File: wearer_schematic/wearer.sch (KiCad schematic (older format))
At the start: 19 parts

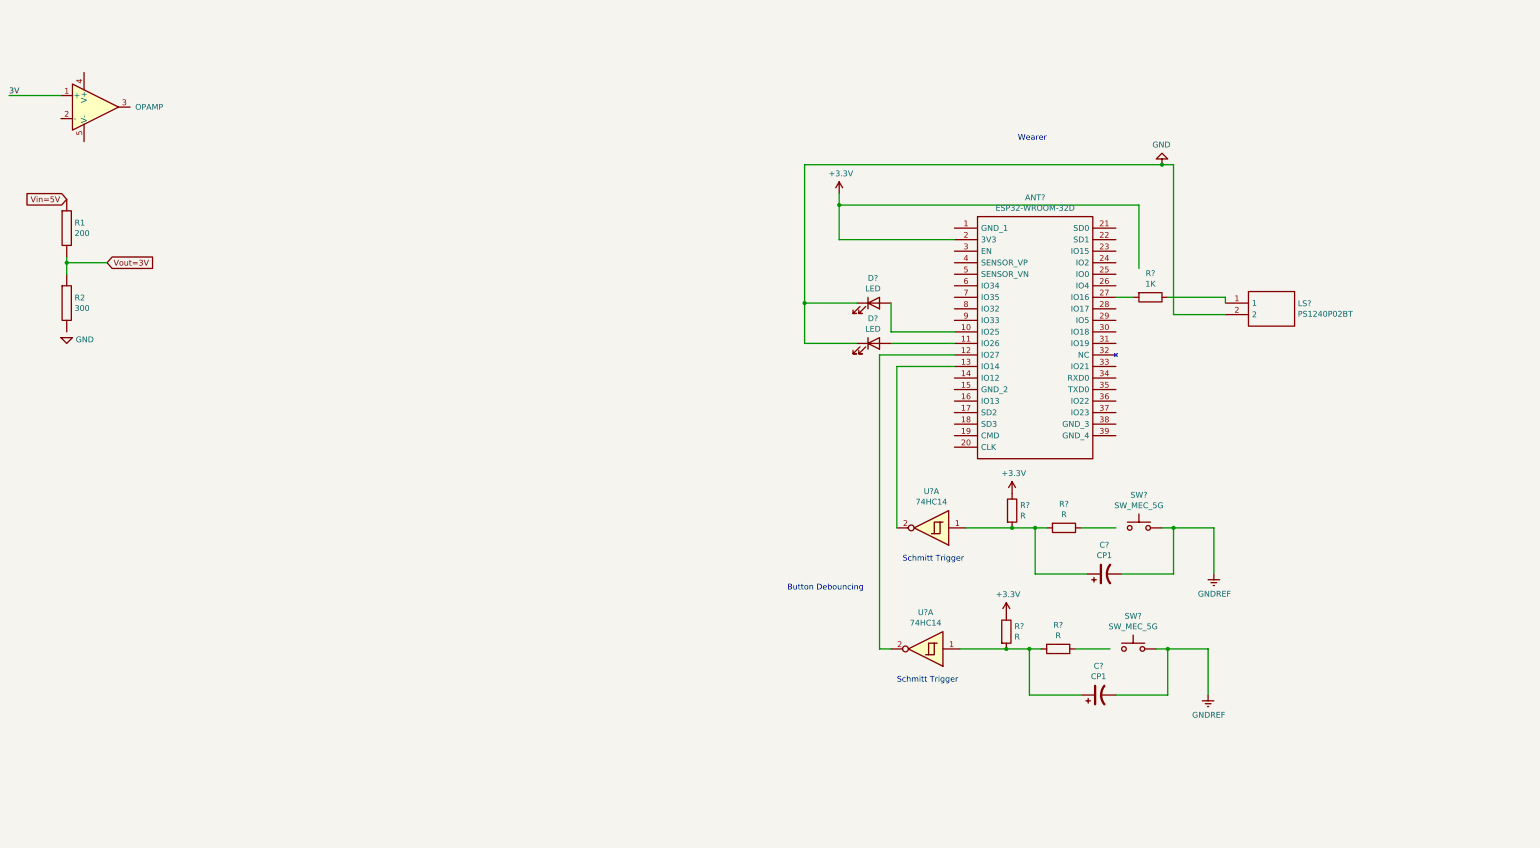
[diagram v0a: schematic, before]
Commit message: added to schematic
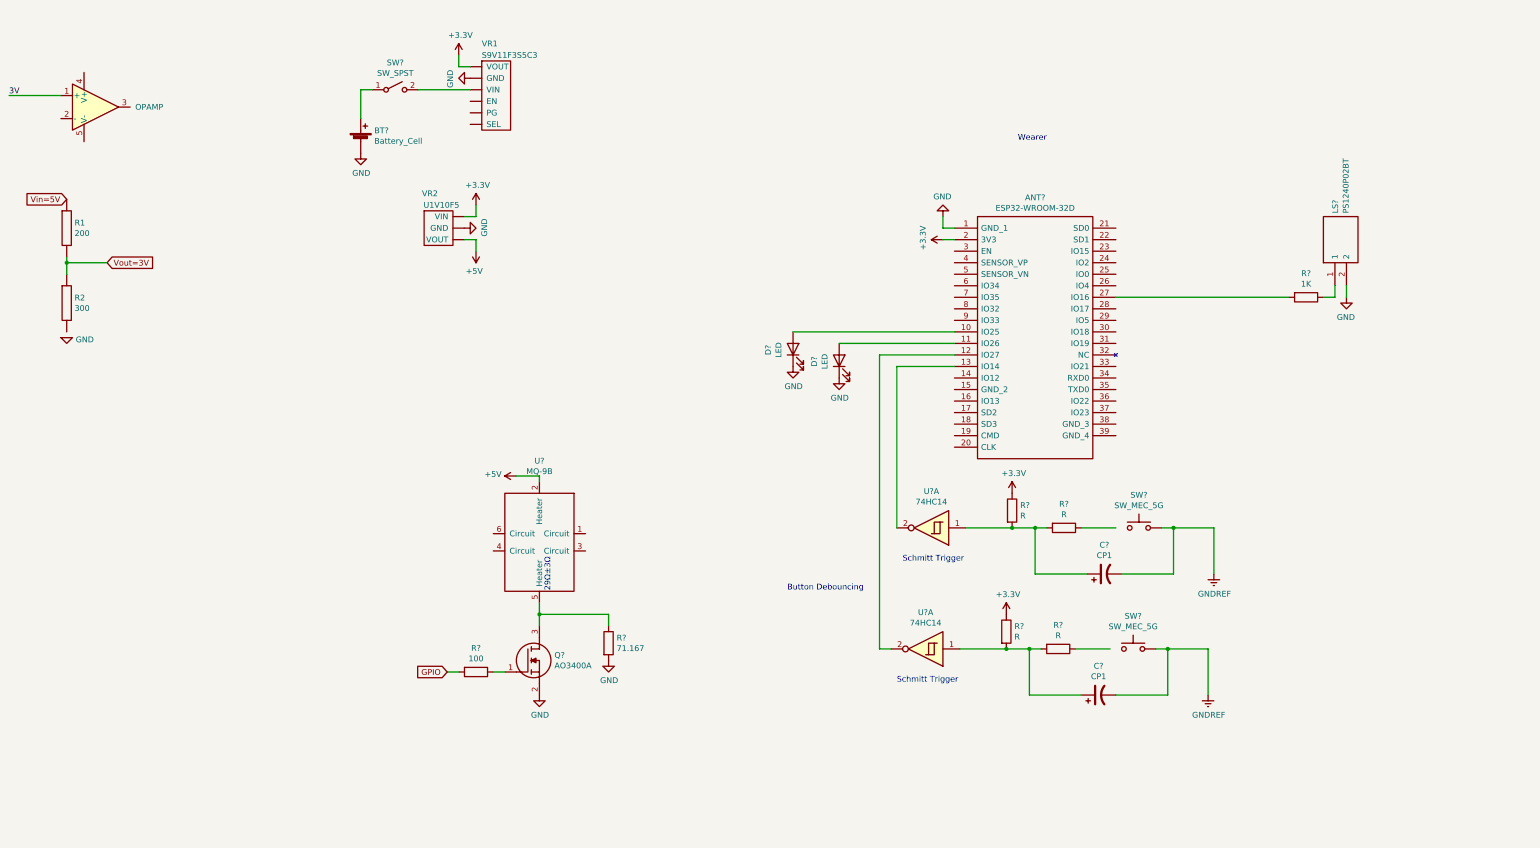
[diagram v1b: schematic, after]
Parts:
- added BT?: Battery_Cell, symbol Device:Battery_Cell
- added Q?: AO3400A, SOT95P280X125-3N, symbol Noggin:AO3400A
- added R?: 100, symbol Device:R
- added R?: 71.167, symbol Device:R
- added SW?: SW_SPST, symbol Switch:SW_SPST
- added U?: MQ-9B, symbol Noggin:MQ-9B
- added VR1: S9V11F3S5C3, symbol Noggin:S9V11F3S5C3
- added VR2: U1V10F5, symbol Noggin:U1V10F5
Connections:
- net +3V3: now also VR1.~ (VOUT), VR2.~ (VOUT)
- net GND: now also ANT?.1 (GND_1), BT?.2 (-), Q?.2, R?.2, VR1.~ (VOUT), VR2.~ (VOUT)
- new net: SW?.2 (B), VR1.~ (VOUT)
- new net: BT?.1 (+), SW?.1 (A)
- new net: Q?.3, R?.1, U?.5 (Heater)
- new net: Q?.1, R?.1
- new net +5V: U?.2 (Heater), VR2.~ (VOUT)
- new net GPIO: R?.2
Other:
- note added: "29Ω±3Ω"
- moved on the sheet: D?, LS?, R?

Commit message: updated wearer schematic
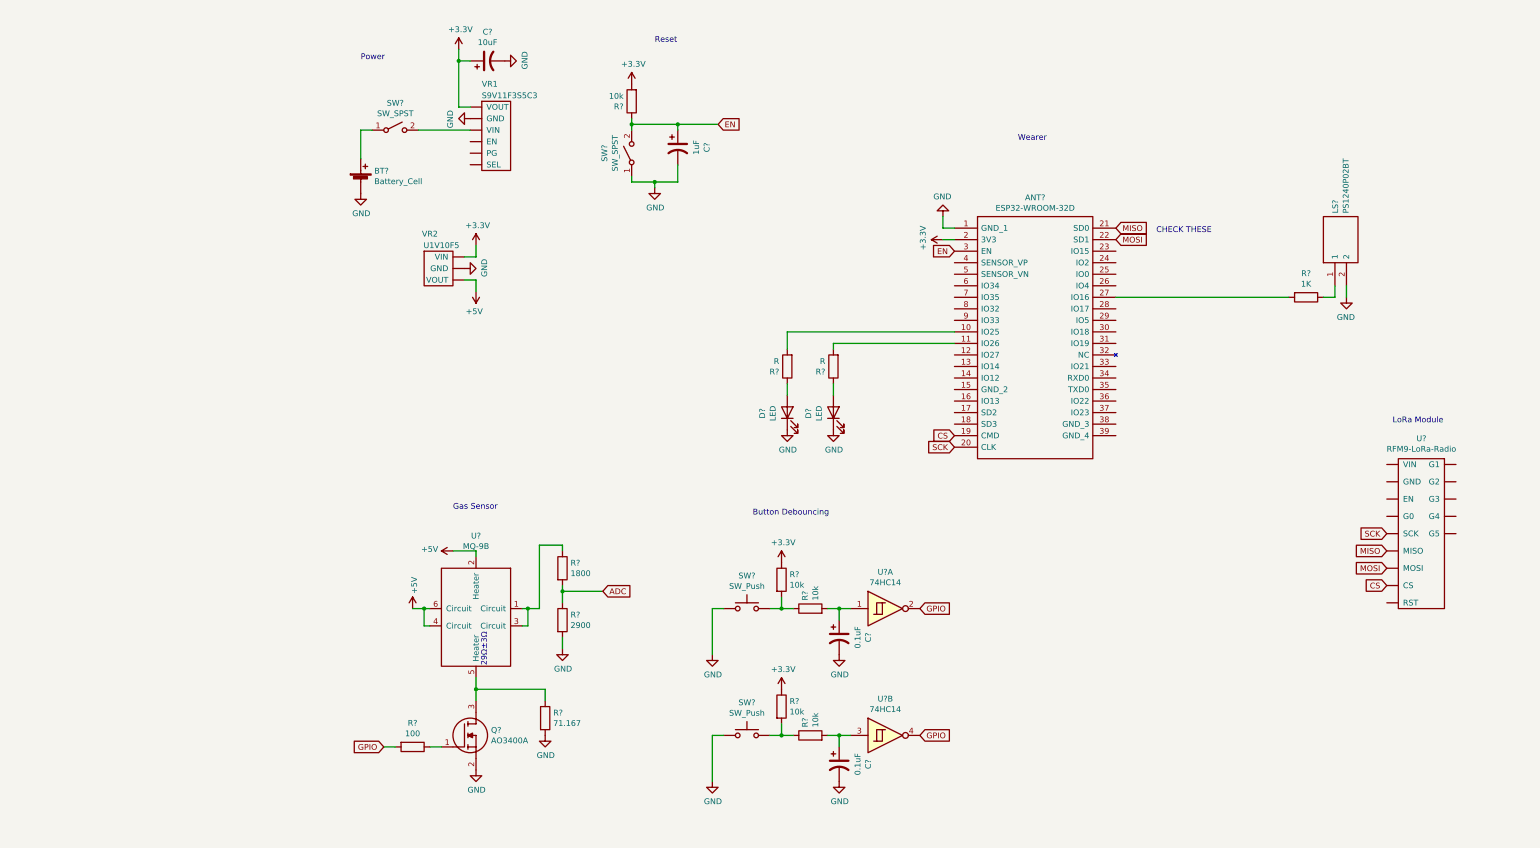
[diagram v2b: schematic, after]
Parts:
- removed C? (x2): CP1, symbol Device:CP1
- removed GND: 0, symbol pspice:0
- removed OpAmp1: OPAMP, symbol pspice:OPAMP
- removed R1: 200, symbol pspice:R
- removed R2: 300, symbol pspice:R
- removed R? (x4): R, symbol Device:R
- removed SW? (x2): SW_MEC_5G, symbol Switch:SW_MEC_5G
- removed U? (x2): 74HC14, symbol 74xx:74HC14
- added C?: 10uF, symbol Device:CP1
- added C? (x2): 0.1uF, symbol Device:CP1
- added C?: 1uF, symbol Device:CP1
- added R? (x2): R, symbol Device:R
- added R?: 1800, symbol Device:R
- added R?: 2900, symbol Device:R
- added R? (x5): 10k, symbol Device:R
- added SW? (x2): SW_Push, symbol Switch:SW_Push
- added SW?: SW_SPST, symbol Switch:SW_SPST
- added U?: RFM9-LoRa-Radio, symbol Noggin:RFM9-LoRa-Radio
- added U? (x2): 74HC14, symbol 74xx:74HC14
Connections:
- net +3V3: now also C?.1, R?.1, R?.1, R?.2
- net +5V: now also U?.4 (Circuit), U?.6 (Circuit)
- net GND: now also C?.2, C?.2, C?.2, C?.2, R?.2, SW?.1, SW?.1, SW?.1 (A)
- net GPIO: now also U?.2, U?.4
- net at ANT?.10 (IO25): now also R?.2; no longer D?.2 (A)
- net at ANT?.11 (IO26): now also R?.2; no longer D?.2 (A)
- net CS: now reaches ANT?.19 (CMD)
- net CS: now also U?.~ (VIN)
- net SCK: now reaches ANT?.20 (CLK)
- net SCK: now also U?.~ (VIN)
- net MISO: now reaches ANT?.21 (SD0)
- net MISO: now also U?.~ (VIN)
- net MOSI: now reaches ANT?.22 (SD1)
- net MOSI: now also U?.~ (VIN)
- net EN: now reaches ANT?.3 (EN)
- net EN: now also C?.1, R?.1, SW?.2 (B)
- net at U?.1 (Circuit): now also U?.3 (Circuit), R?.1
- new net: D?.2 (A), R?.1 (x2)
- new net: C?.1, R?.2, U?.1
- new net: C?.1, R?.2, U?.3
- new net: R?.1, R?.2, SW?.2 (x2)
- new net ADC: R?.1, R?.2
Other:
- note added: "Button Debouncing"
- note added: "CHECK THESE"
- note added: "Gas Sensor"
- note added: "LoRa Module"
- note added: "Power"
- note added: "Reset"
- note removed: "Button Debouncing\n"
- note removed: "Schmitt Trigger\n"
- moved on the sheet: BT?, D?, Q?, R?, SW?, U?, VR1, VR2

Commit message: update schematic
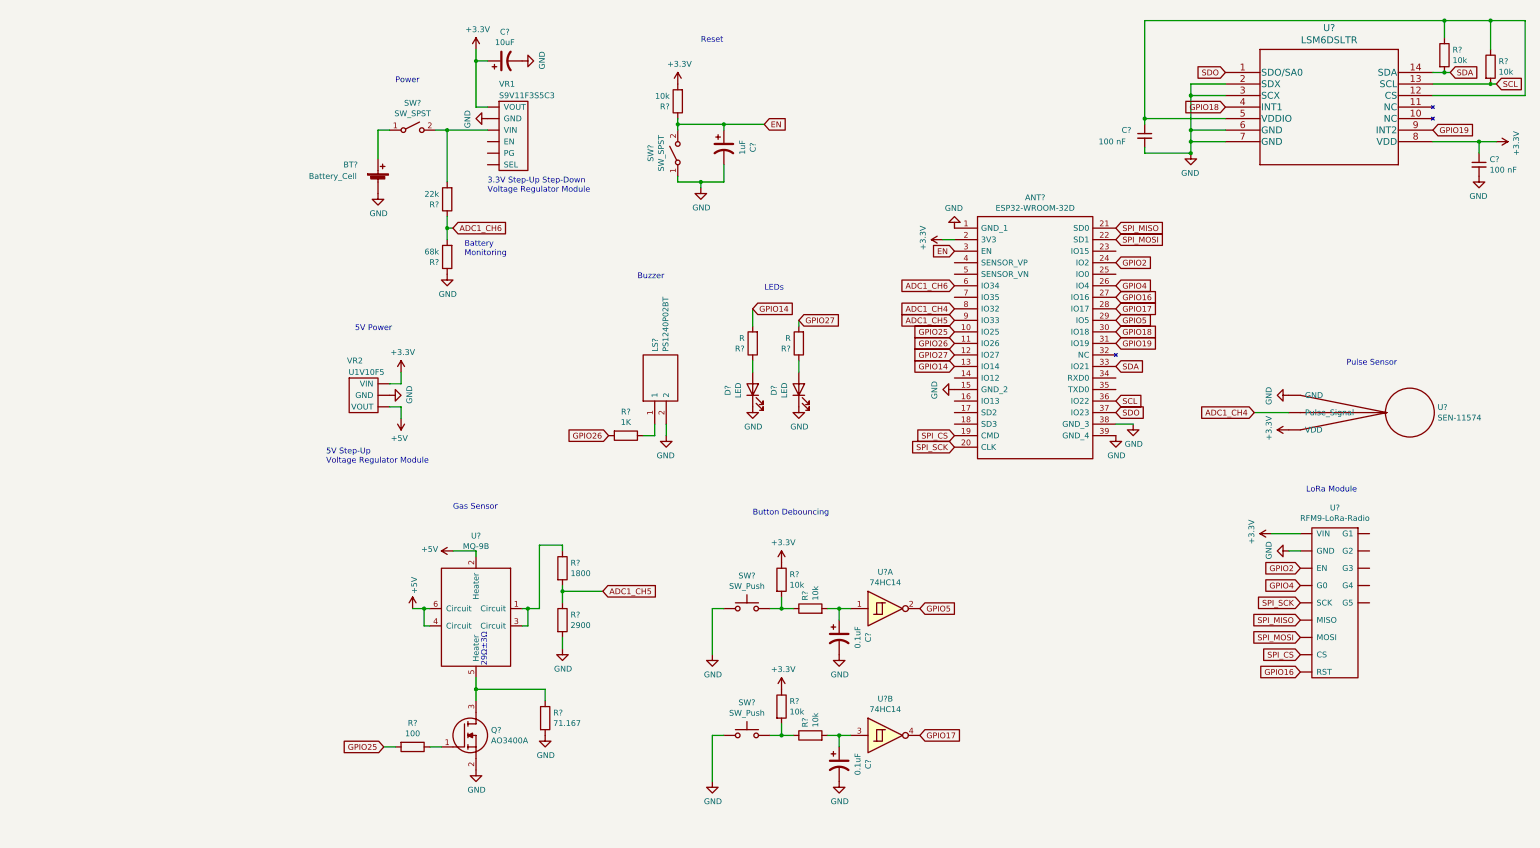
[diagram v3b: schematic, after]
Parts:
- added C? (x2): 100 nF, symbol Device:C_Small
- added R? (x2): 10k, symbol Device:R
- added R?: 22k, symbol Device:R
- added R?: 68k, symbol Device:R
- added U?: LSM6DSLTR, QFN_6DSLTR_STM, symbol Noggin:LSM6DSLTR
- added U?: SEN-11574, symbol Noggin:SEN-11574
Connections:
- net ADC is gone; now on net ADC1_CH5: R?.1, R?.2
- net SCK is gone; now on net SPI_SCK: ANT?.20 (CLK), U?.~ (VIN)
- net +3V3: now also U?.~ (VIN), C?.1, U?.8 (VDD), U?.~ (VDD)
- net GND: now also ANT?.15 (GND_2), ANT?.38 (GND_3), ANT?.39 (GND_4), U?.~ (VIN), C?.2, C?.2, R?.1, U?.2 (SDX), U?.3 (SCX), U?.6 (GND), U?.7 (GND), U?.~ (VDD)
- net GPIO14: now reaches R?.2
- net GPIO14: now also ANT?.13 (IO14); no longer ANT?.10 (IO25)
- net GPIO26: now reaches ANT?.11 (IO26)
- net GPIO26: now also R?.2; no longer R?.2
- net GPIO27: now reaches ANT?.12 (IO27)
- net GPIO27: now also R?.2
- net GPIO2: now reaches ANT?.24 (IO2)
- net GPIO2: now also U?.~ (VIN)
- net GPIO4: now reaches ANT?.26 (IO4)
- net GPIO4: now also U?.~ (VIN)
- net GPIO16: now reaches ANT?.27 (IO16)
- net GPIO16: now also U?.~ (VIN); no longer R?.2
- net GPIO17: now reaches ANT?.28 (IO17)
- net GPIO17: now also U?.4
- net GPIO5: now reaches ANT?.29 (IO5)
- net GPIO5: now also U?.2
- net GPIO18: now reaches ANT?.30 (IO18)
- net GPIO18: now also U?.4 (INT1)
- net GPIO19: now reaches ANT?.31 (IO19)
- net GPIO19: now also U?.9 (INT2)
- net SDA: now reaches ANT?.33 (IO21)
- net SDA: now also R?.2, U?.14 (SDA)
- net SCL: now reaches ANT?.36 (IO22)
- net SCL: now also R?.2, U?.13 (SCL)
- net SDO: now reaches ANT?.37 (IO23)
- net SDO: now also U?.1 (SDO/SA0)
- net ADC1_CH6: now reaches ANT?.6 (IO34)
- net ADC1_CH6: now also R?.1, R?.2
- net ADC1_CH4: now reaches ANT?.8 (IO32)
- net ADC1_CH4: now also U?.~ (VDD)
- net ADC1_CH5: now reaches ANT?.9 (IO33)
- net at SW?.2 (B), VR1.~ (VOUT): now also R?.2
- net SPI_SCK: now reaches U?.~ (VIN)
- net CS renamed SPI_CS
- removed net GPIO: R?.2, U?.2, U?.4
- net MISO renamed SPI_MISO
- net MOSI renamed SPI_MOSI
- new net: C?.1, R?.1, R?.1, U?.12 (CS), U?.5 (VDDIO)
- new net GPIO25: ANT?.10 (IO25), R?.2
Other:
- note added: "3.3V Step-Up Step-Down\nVoltage Regulator Module"
- note added: "5V Power"
- note added: "5V Step-Up\nVoltage Regulator Module"
- note added: "Battery\nMonitoring"
- note added: "Buzzer"
- note added: "LEDs"
- note added: "Pulse Sensor"
- note removed: "CHECK THESE"
- note removed: "Wearer\n"
- moved on the sheet: BT?, C?, D?, LS?, R?, SW?, U?, VR1, VR2

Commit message: update debouncing
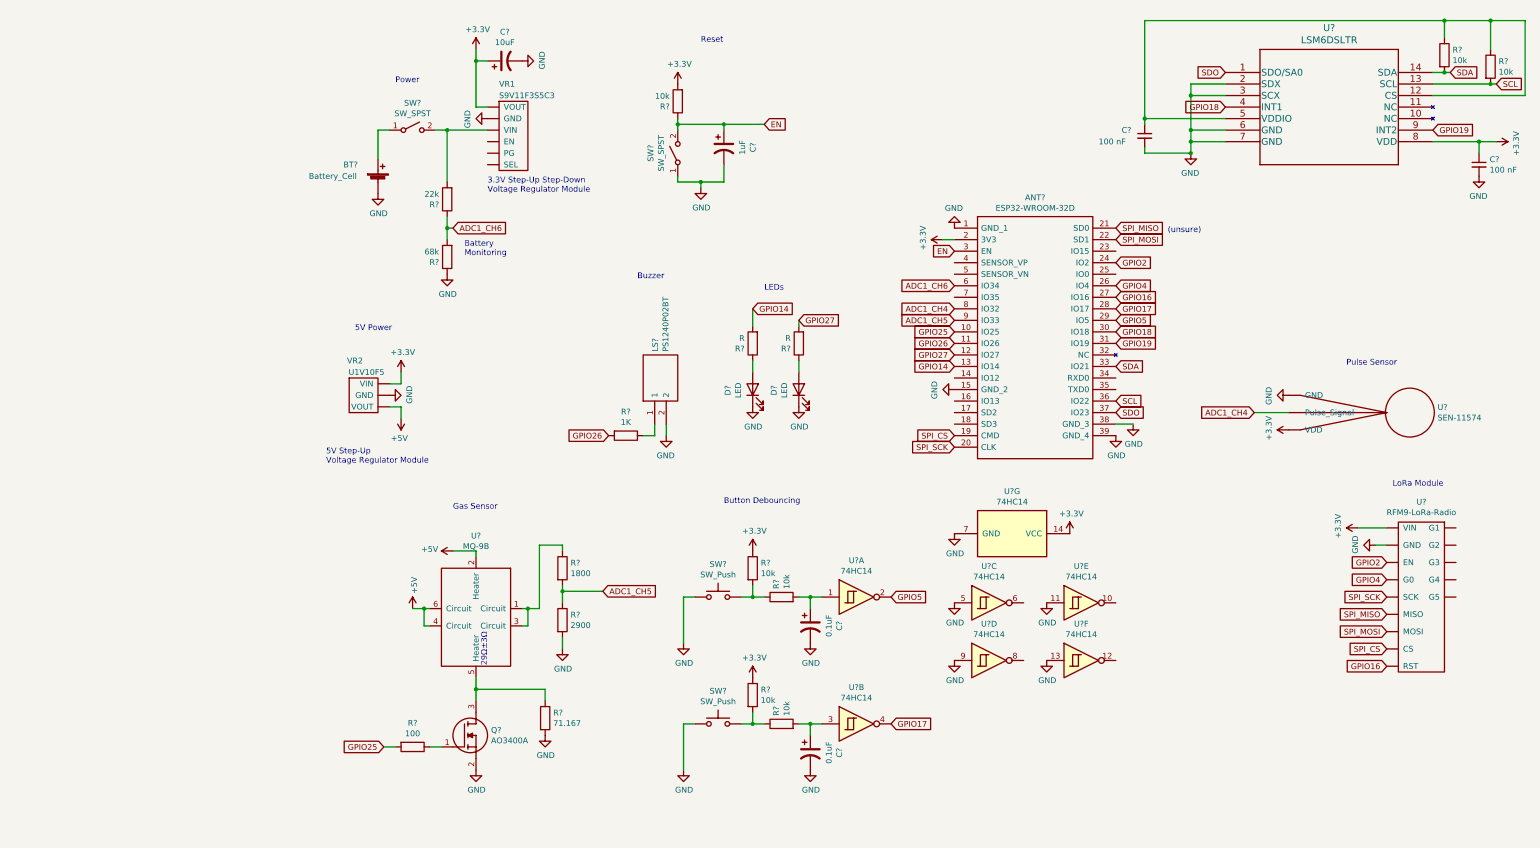
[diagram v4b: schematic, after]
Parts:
- added U? (x5): 74HC14, symbol 74xx:74HC14
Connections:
- net +3V3: now also U?.14 (VCC)
- net GND: now also U?.11, U?.13, U?.5, U?.7 (GND), U?.9
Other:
- note added: "(unsure)"
- moved on the sheet: C?, R?, SW?, U?, U?A, U?B

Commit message: add espflasher
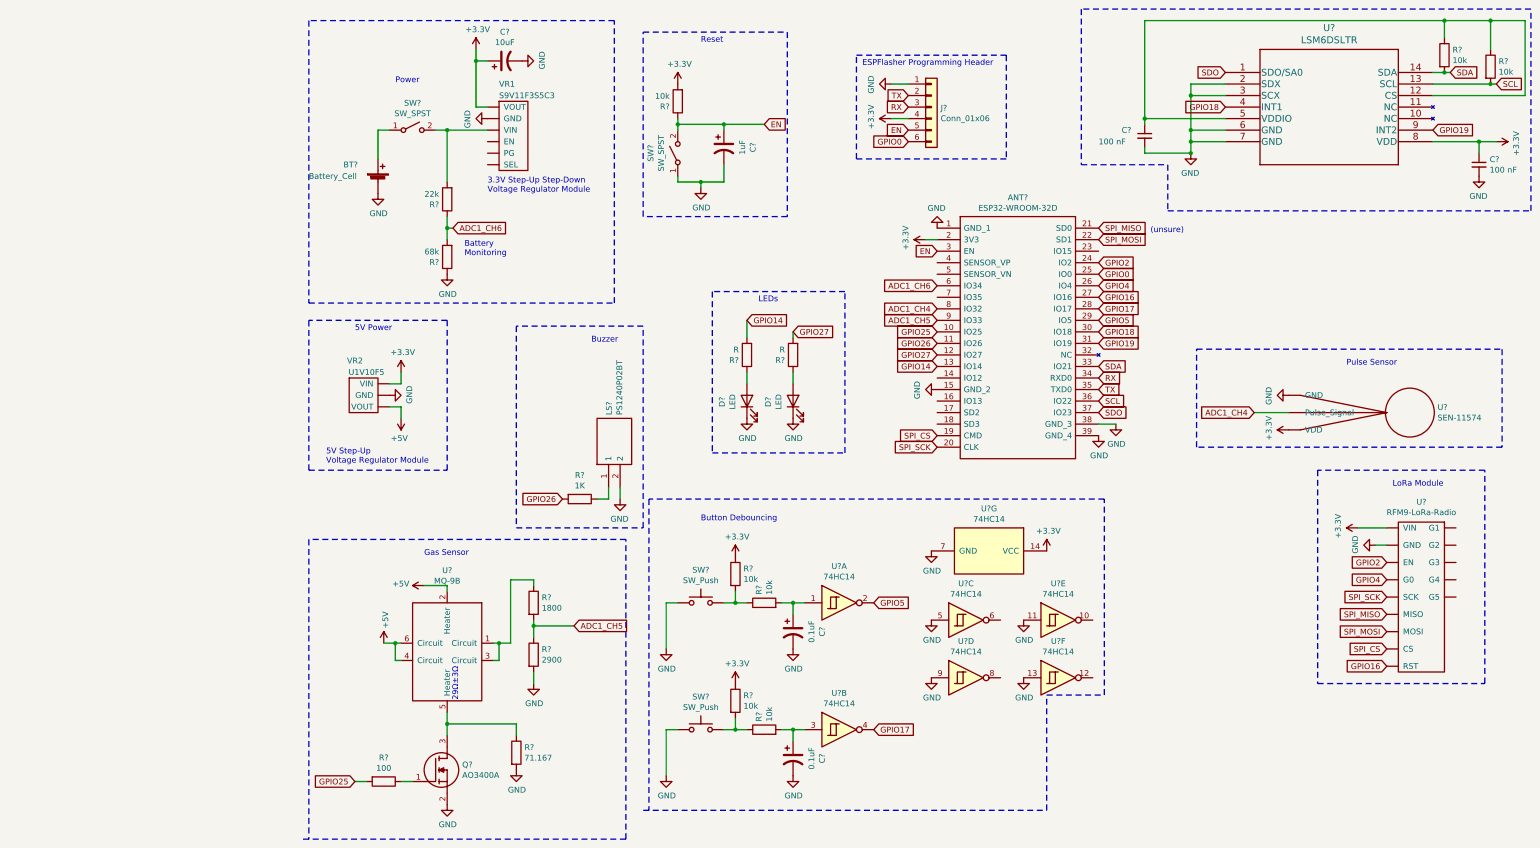
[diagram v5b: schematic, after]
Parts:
- added J?: Conn_01x06, symbol Connector_Generic:Conn_01x06
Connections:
- net +3V3: now also J?.4 (Pin_4)
- net EN: now also J?.5 (Pin_5)
- net GND: now also J?.1 (Pin_1)
- net GPIO0: now reaches ANT?.25 (IO0)
- net GPIO0: now also J?.6 (Pin_6)
- net RX: now reaches ANT?.34 (RXD0)
- net RX: now also J?.3 (Pin_3)
- net TX: now reaches ANT?.35 (TXD0)
- net TX: now also J?.2 (Pin_2)
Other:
- note added: "ESPFlasher Programming Header"
- moved on the sheet: ANT?, C?, D?, LS?, Q?, R?, SW?, U?, U?A, U?B, U?C, U?D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
